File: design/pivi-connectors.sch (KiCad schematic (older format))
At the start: 15 parts, among them P2 CONN_01X02, P3 Recom_Power_RAC10-05SC/277, P5 CONN_02X20, P6 CONN_01X04

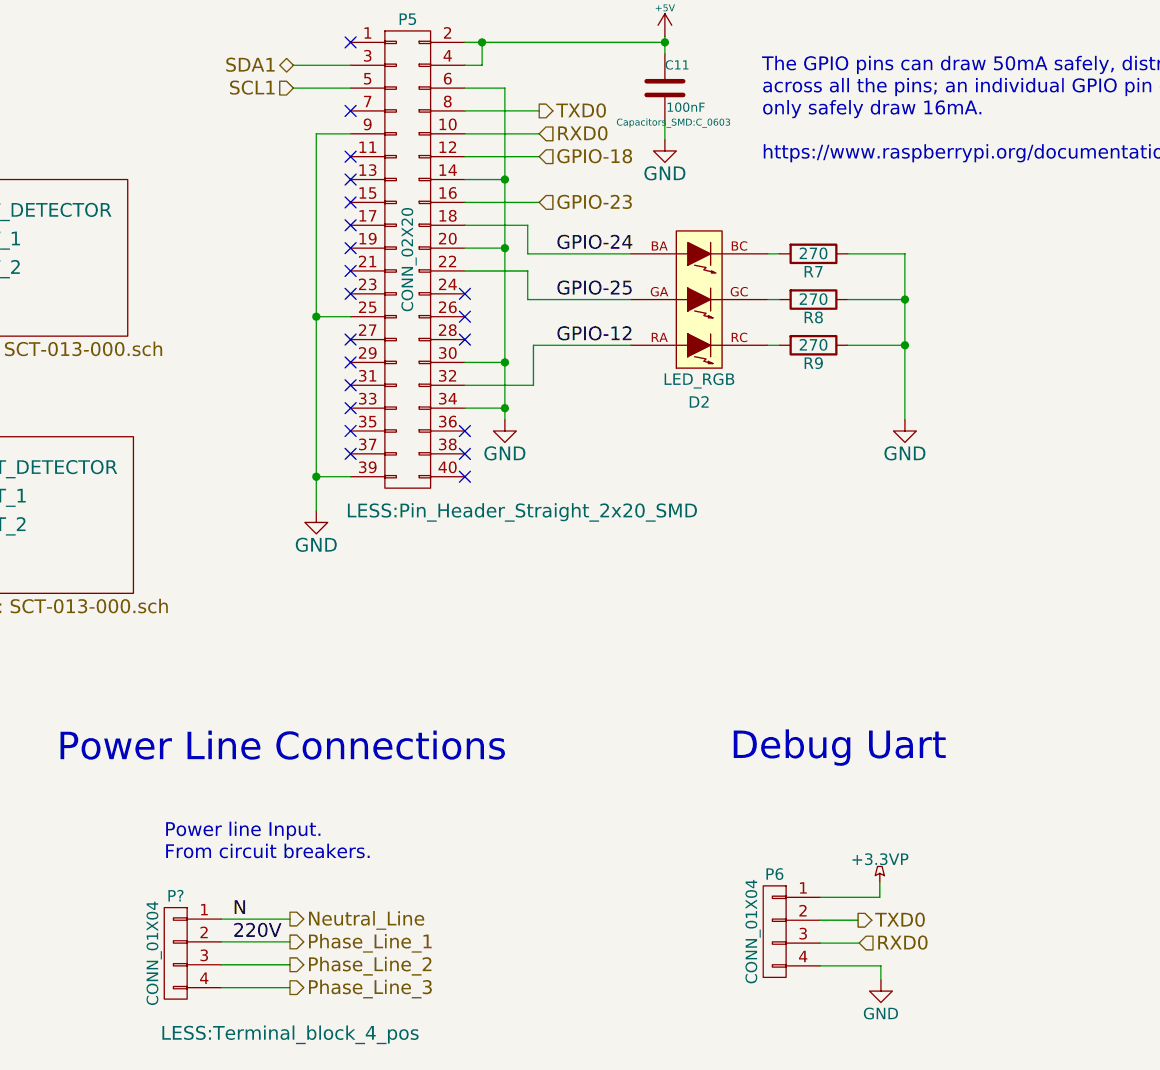
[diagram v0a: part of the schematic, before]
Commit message: Correct minor problem in LED RGB library.
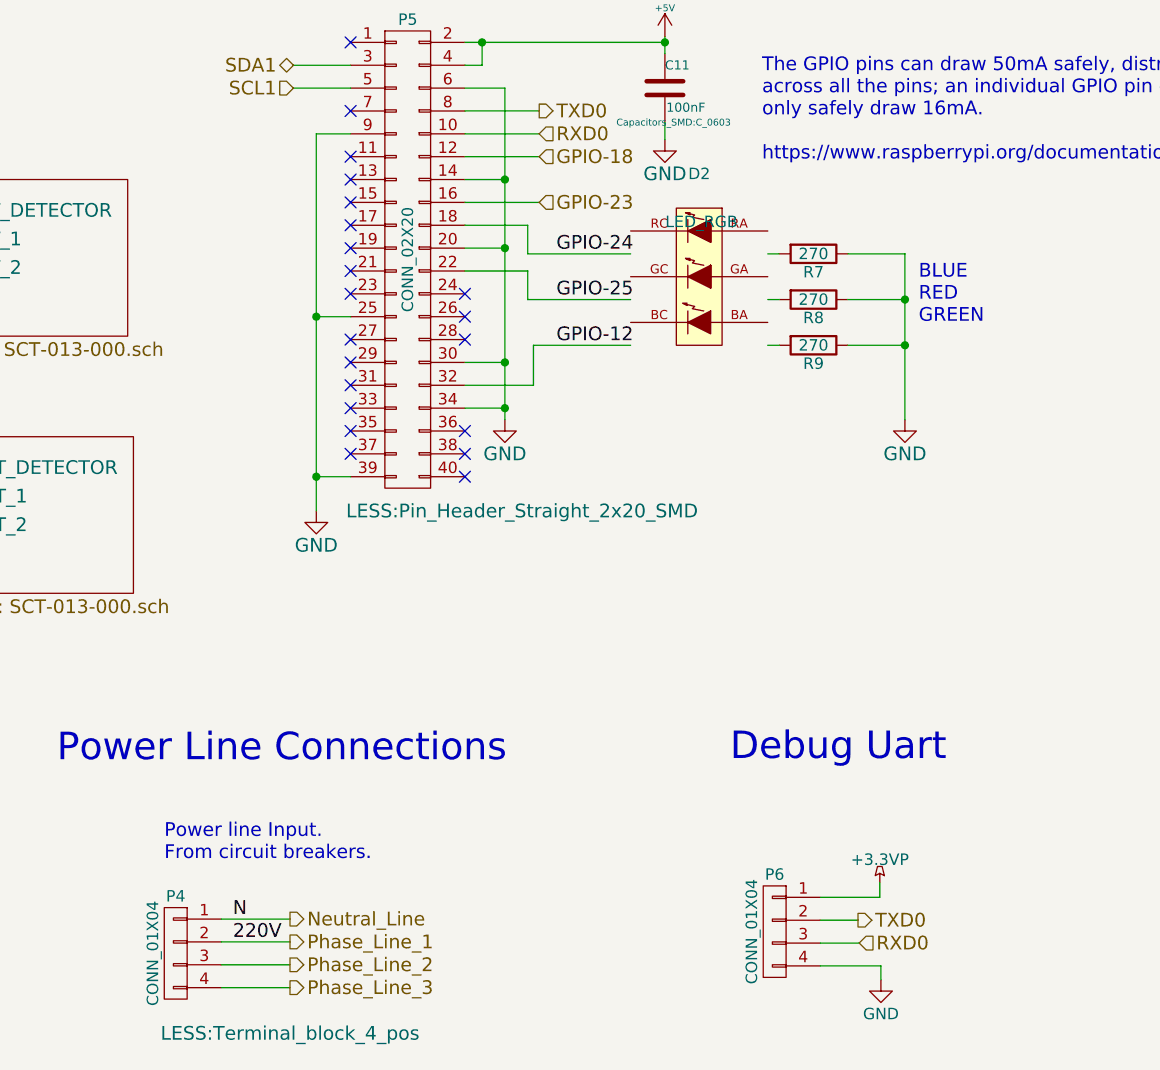
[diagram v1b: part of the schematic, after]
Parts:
- gave numbers to parts that had none: 1
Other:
- note added: "BLUE\nRED\nGREEN"
- moved on the sheet: D2
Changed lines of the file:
@@
 L LED_RGB D2
 U 1 1 55BA51D0
-P 8540 2390
-F 0 "D2" H 8540 2840 50  0000 C CNN
-F 1 "LED_RGB" H 8540 2740 50  0000 C CNN
-F 2 "LEDs:LED_RGB_PLLC-6" H 8540 2340 60  0001 C CNN
-F 3 "" H 8540 2340 60  0000 C CNN
-	1    8540 2390
-	-1   0    0    1
+P 8540 2290
+F 0 "D2" H 8540 2740 50  0000 C CNN
+F 1 "LED_RGB" H 8550 2530 50  0000 C CNN
+F 2 "LEDs:LED_RGB_PLLC-6" H 8540 2240 60  0001 C CNN
+F 3 "" H 8540 2240 60  0000 C CNN
+	1    8540 2290
+	1    0    0    -1
 $EndComp
 $Comp
@@
 Phase_Line_3
 $Comp
-L CONN_01X04 P?
+L CONN_01X04 P4
 U 1 1 55F7C621
 P 6250 5250
-F 0 "P?" H 6250 5500 50  0000 C CNN
+F 0 "P4" H 6250 5500 50  0000 C CNN
 F 1 "CONN_01X04" V 6350 5250 50  0000 C CNN
 F 2 "LESS:Terminal_block_4_pos" H 5750 4900 60  0000 C CNN
@@
 Wire Wire Line
 	6450 5400 6750 5400
+Text Notes 9500 2500 0    60   ~ 0
+BLUE\nRED\nGREEN
 $EndSCHEMATC

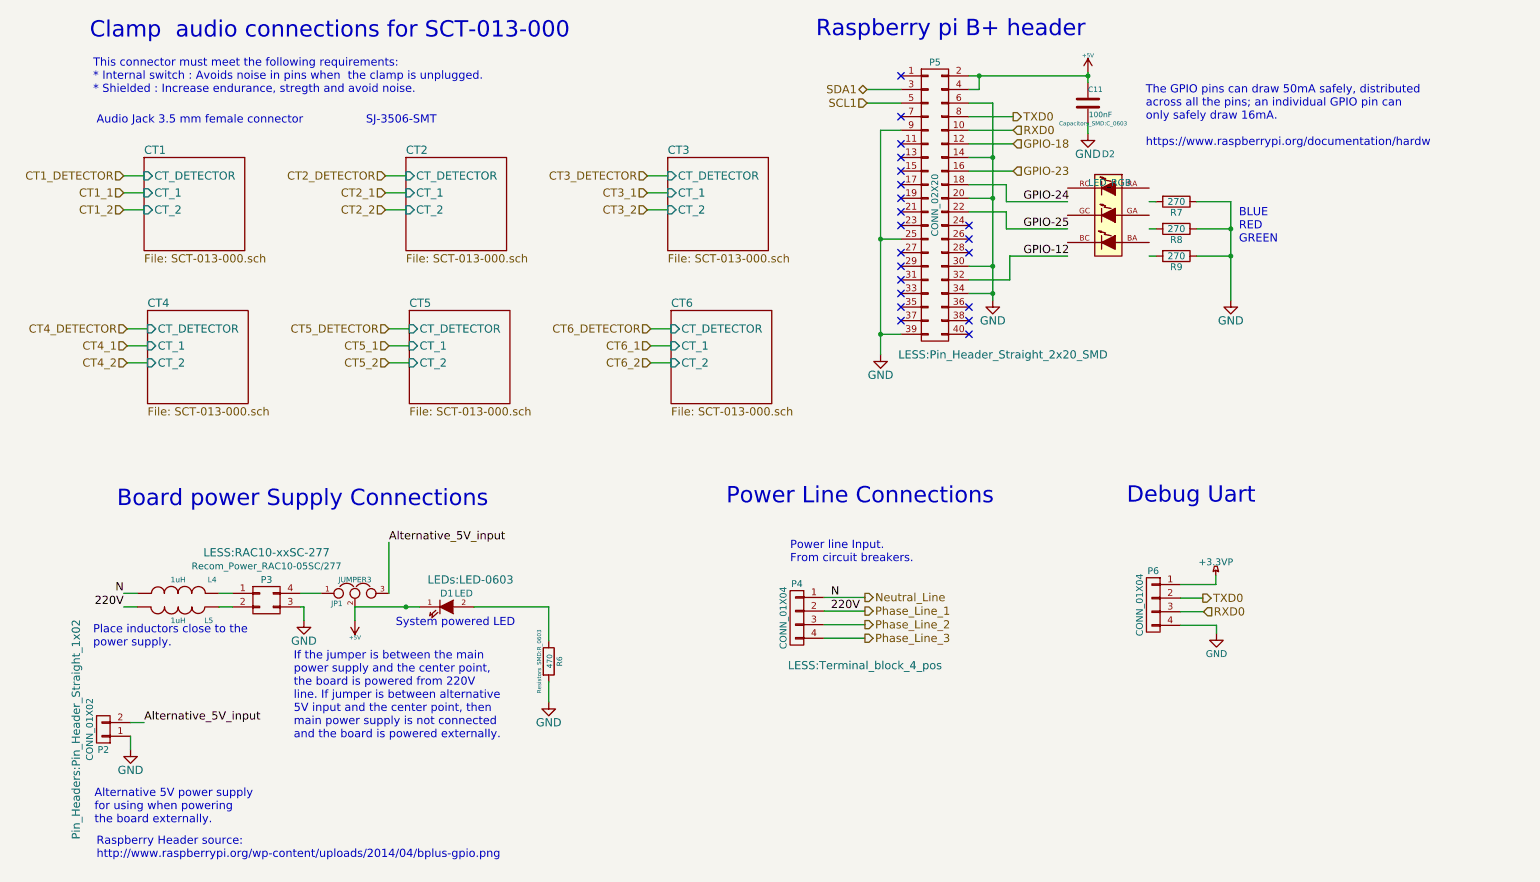
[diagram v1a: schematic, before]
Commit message: Fix #7, Fix #8, Fix #9, Fix #10, Fix #11
Several fixes improvements:
* Fix #7: Add 2mm idle to each side of the connector.
* Fix #8: Add 0.25mm to each side of the connector.
* Fix #9: Mirror component. Checked with the datasheet.
* Fix #10: correct label name.
* Fix #11: Changed the terminal block for one with a better mouting system.

Also check the Raspberry pi 20 pin header. It is place in the correct position.
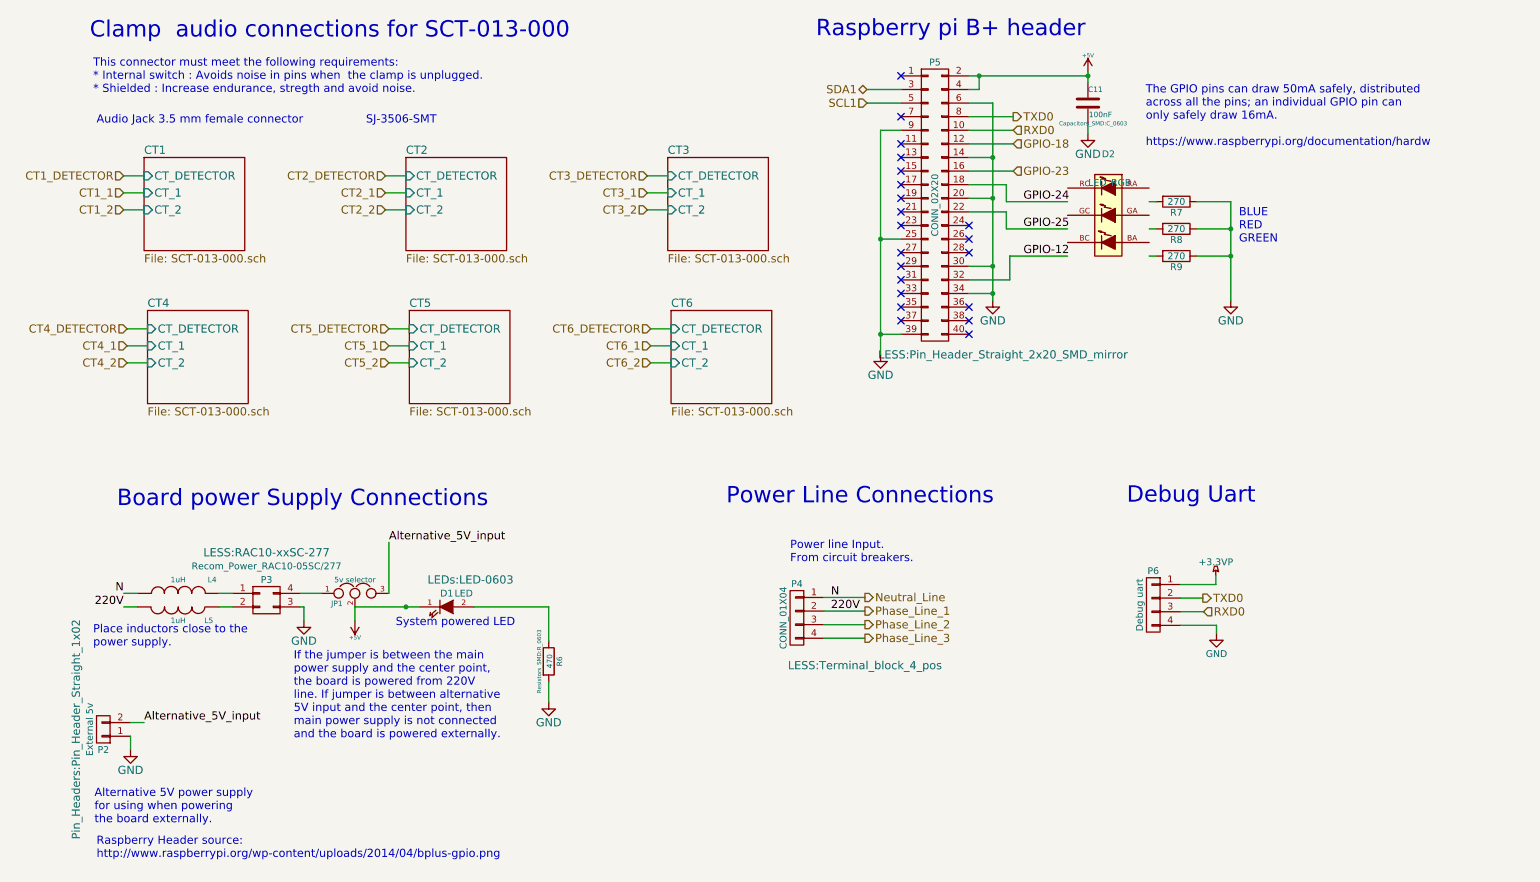
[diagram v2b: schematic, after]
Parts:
- JP1: value JUMPER3 -> 5v selector
- P2: value CONN_01X02 -> External 5v
- P5: footprint LESS:Pin_Header_Straight_2x20_SMD -> LESS:Pin_Header_Straight_2x20_SMD_mirror
- P6: value CONN_01X04 -> Debug uart
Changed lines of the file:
@@
 F 0 "P5" H 7265 3265 50  0000 C CNN
 F 1 "CONN_02X20" V 7265 2215 50  0000 C CNN
-F 2 "LESS:Pin_Header_Straight_2x20_SMD" H 7765 1115 60  0000 C CNN
+F 2 "LESS:Pin_Header_Straight_2x20_SMD_mirror" H 7765 1115 60  0000 C CNN
 F 3 "" H 7265 1265 60  0000 C CNN
 	1    7265 2215
@@
 P 1150 6070
 F 0 "P2" H 1150 6220 50  0000 C CNN
-F 1 "CONN_01X02" V 1250 6070 50  0000 C CNN
+F 1 "External 5v" V 1250 6070 50  0000 C CNN
 F 2 "Pin_Headers:Pin_Header_Straight_1x02" V 1350 6070 60  0000 C CNN
 F 3 "" H 1150 6070 60  0000 C CNN
@@
 P 3000 5070
 F 0 "JP1" H 2825 4995 40  0000 L CNN
-F 1 "JUMPER3" H 3000 5170 40  0000 C CNN
+F 1 "5v selector" H 3000 5170 40  0000 C CNN
 F 2 "Pin_Headers:Pin_Header_Straight_1x03" H 3000 5070 60  0001 C CNN
 F 3 "" H 3000 5070 60  0000 C CNN
@@
 P 8870 5155
 F 0 "P6" H 8870 5405 50  0000 C CNN
-F 1 "CONN_01X04" V 8970 5155 50  0000 C CNN
+F 1 "Debug uart" V 8970 5155 50  0000 C CNN
 F 2 "Pin_Headers:Pin_Header_Straight_1x04" H 8870 5155 60  0001 C CNN
 F 3 "" H 8870 5155 60  0000 C CNN

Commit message: PIVI version 2.1 routed.
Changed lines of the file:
@@
 LIBS:txs0104e
 LIBS:less
+LIBS:RGB-LED-PLL6
 EELAYER 25 0
 EELAYER END
@@
 GPIO-23
 $Comp
-L LED_RGB D2
-U 1 1 55BA51D0
-P 8540 2290
-F 0 "D2" H 8540 2740 50  0000 C CNN
-F 1 "LED_RGB" H 8550 2530 50  0000 C CNN
-F 2 "LEDs:LED_RGB_PLLC-6" H 8540 2240 60  0001 C CNN
-F 3 "" H 8540 2240 60  0000 C CNN
-	1    8540 2290
-	1    0    0    -1
-$EndComp
-$Comp
 L R R7
 U 1 1 55BA6452
@@
 Text Notes 9500 2500 0    60   ~ 0
 BLUE\nRED\nGREEN
+$Comp
+L LED_RGB D2
+U 1 1 55F5FF1D
+P 8540 2390
+F 0 "D2" H 8540 2840 50  0000 C CNN
+F 1 "LED_RGB" H 8540 2740 50  0000 C CNN
+F 2 "LEDs:LED_RGB_PLLC-6" H 8540 2340 60  0000 C CNN
+F 3 "" H 8540 2340 60  0000 C CNN
+	1    8540 2390
+	-1   0    0    1
+$EndComp
 $EndSCHEMATC
